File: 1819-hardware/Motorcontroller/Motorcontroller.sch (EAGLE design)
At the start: 34 parts, among them U1 GENERIC-SOIC8MSGEQ7N-FILTER, U2 GENERIC-SOIC8MSGEQ7N-FILTER, U3 GENERIC-SOIC8MSGEQ7N-FILTER

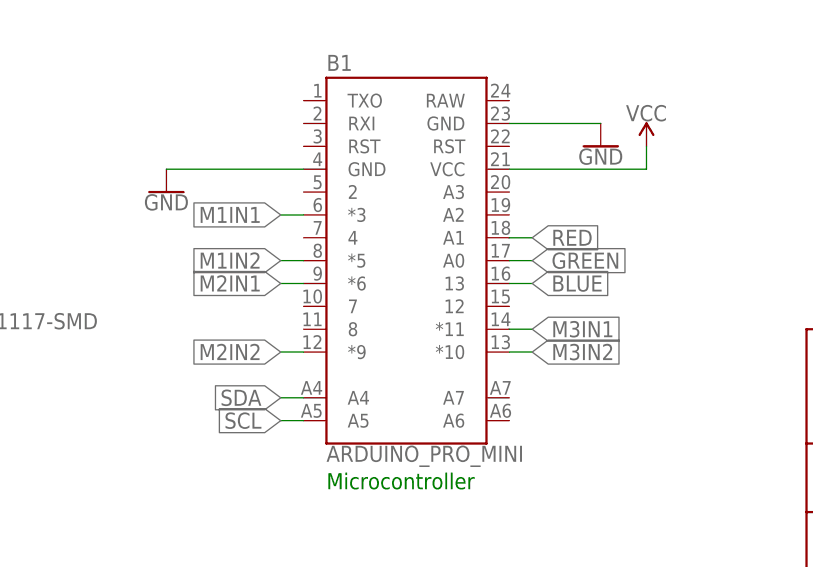
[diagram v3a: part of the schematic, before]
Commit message: the arduino was upside down
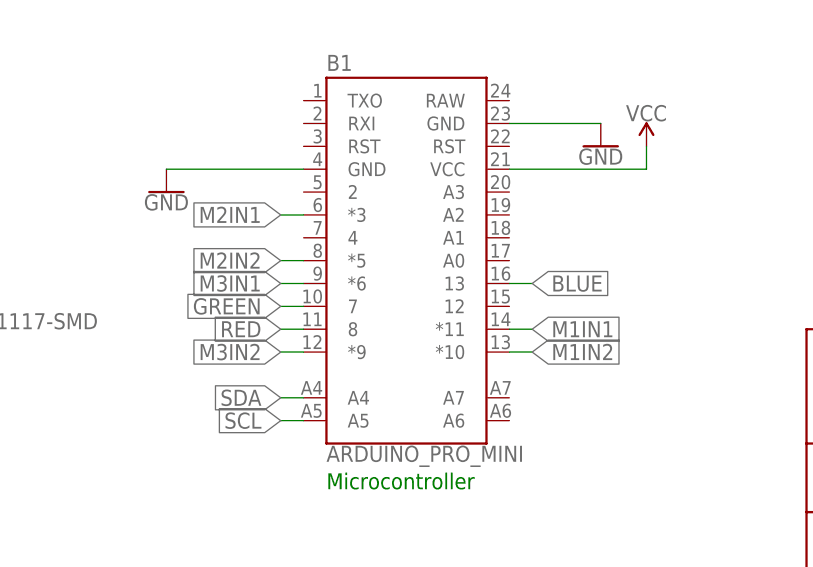
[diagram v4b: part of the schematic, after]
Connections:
- net GREEN: now also B1.7; no longer B1.A0
- net M1IN1: now also B1.*11; no longer B1.*3
- net M1IN2: now also B1.*10; no longer B1.*5
- net M2IN1: now also B1.*3; no longer B1.*6
- net M2IN2: now also B1.*5; no longer B1.*9
- net M3IN1: now also B1.*6; no longer B1.*11
- net M3IN2: now also B1.*9; no longer B1.*10
- net RED: now also B1.8; no longer B1.A1
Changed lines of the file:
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@@
 </segment>
 <segment>
-<pinref part="B1" gate="G$1" pin="A1"/>
-<wire x1="114.3" y1="45.72" x2="116.84" y2="45.72" width="0.1524" layer="91"/>
-<label x="116.84" y="45.72" size="1.778" layer="95" xref="yes"/>
+<pinref part="B1" gate="G$1" pin="8"/>
+<wire x1="91.44" y1="35.56" x2="88.9" y2="35.56" width="0.1524" layer="91"/>
+<label x="88.9" y="35.56" size="1.778" layer="95" rot="R180" xref="yes"/>
 </segment>
 </net>
@@
 </segment>
 <segment>
-<pinref part="B1" gate="G$1" pin="A0"/>
-<wire x1="114.3" y1="43.18" x2="116.84" y2="43.18" width="0.1524" layer="91"/>
-<label x="116.84" y="43.18" size="1.778" layer="95" xref="yes"/>
+<pinref part="B1" gate="G$1" pin="7"/>
+<wire x1="91.44" y1="38.1" x2="88.9" y2="38.1" width="0.1524" layer="91"/>
+<label x="88.9" y="38.1" size="1.778" layer="95" rot="R180" xref="yes"/>
 </segment>
 </net>
@@
 <net name="M1IN1" class="0">
 <segment>
-<pinref part="B1" gate="G$1" pin="*3"/>
-<wire x1="91.44" y1="48.26" x2="88.9" y2="48.26" width="0.1524" layer="91"/>
-<label x="88.9" y="48.26" size="1.778" layer="95" rot="R180" xref="yes"/>
-</segment>
-<segment>
 <pinref part="U1" gate="G$1" pin="3"/>
 <wire x1="177.8" y1="162.56" x2="175.26" y2="162.56" width="0.1524" layer="91"/>
 <label x="175.26" y="162.56" size="1.778" layer="95" rot="R180" xref="yes"/>
 </segment>
+<segment>
+<pinref part="B1" gate="G$1" pin="*11"/>
+<wire x1="114.3" y1="35.56" x2="116.84" y2="35.56" width="0.1524" layer="91"/>
+<label x="116.84" y="35.56" size="1.778" layer="95" xref="yes"/>
+</segment>
 </net>
 <net name="M1IN2" class="0">
-<segment>
-<pinref part="B1" gate="G$1" pin="*5"/>
-<wire x1="91.44" y1="43.18" x2="88.9" y2="43.18" width="0.1524" layer="91"/>
-<label x="88.9" y="43.18" size="1.778" layer="95" rot="R180" xref="yes"/>
-</segment>
 <segment>
 <pinref part="U1" gate="G$1" pin="2"/>
@@
 <label x="175.26" y="165.1" size="1.778" layer="95" rot="R180" xref="yes"/>
 </segment>
+<segment>
+<pinref part="B1" gate="G$1" pin="*10"/>
+<wire x1="114.3" y1="33.02" x2="116.84" y2="33.02" width="0.1524" layer="91"/>
+<label x="116.84" y="33.02" size="1.778" layer="95" xref="yes"/>
+</segment>
 </net>
 <net name="M2IN1" class="0">
-<segment>
-<pinref part="B1" gate="G$1" pin="*6"/>
-<wire x1="91.44" y1="40.64" x2="88.9" y2="40.64" width="0.1524" layer="91"/>
-<label x="88.9" y="40.64" size="1.778" layer="95" rot="R180" xref="yes"/>
-</segment>
 <segment>
 <pinref part="U2" gate="G$1" pin="3"/>
@@
 <label x="175.26" y="119.38" size="1.778" layer="95" rot="R180" xref="yes"/>
 </segment>
+<segment>
+<pinref part="B1" gate="G$1" pin="*3"/>
+<wire x1="91.44" y1="48.26" x2="88.9" y2="48.26" width="0.1524" layer="91"/>
+<label x="88.9" y="48.26" size="1.778" layer="95" rot="R180" xref="yes"/>
+</segment>
 </net>
 <net name="M2IN2" class="0">
-<segment>
-<pinref part="B1" gate="G$1" pin="*9"/>
-<wire x1="91.44" y1="33.02" x2="88.9" y2="33.02" width="0.1524" layer="91"/>
-<label x="88.9" y="33.02" size="1.778" layer="95" rot="R180" xref="yes"/>
-</segment>
 <segment>
 <pinref part="U2" gate="G$1" pin="2"/>
 <wire x1="177.8" y1="121.92" x2="175.26" y2="121.92" width="0.1524" layer="91"/>
 <label x="175.26" y="121.92" size="1.778" layer="95" rot="R180" xref="yes"/>
+</segment>
+<segment>
+<pinref part="B1" gate="G$1" pin="*5"/>
+<wire x1="91.44" y1="43.18" x2="88.9" y2="43.18" width="0.1524" layer="91"/>
+<label x="88.9" y="43.18" size="1.778" layer="95" rot="R180" xref="yes"/>
 </segment>
 </net>
@@
 </segment>
 <segment>
-<pinref part="B1" gate="G$1" pin="*11"/>
-<wire x1="114.3" y1="35.56" x2="116.84" y2="35.56" width="0.1524" layer="91"/>
-<label x="116.84" y="35.56" size="1.778" layer="95" xref="yes"/>
+<pinref part="B1" gate="G$1" pin="*6"/>
+<wire x1="91.44" y1="40.64" x2="88.9" y2="40.64" width="0.1524" layer="91"/>
+<label x="88.9" y="40.64" size="1.778" layer="95" rot="R180" xref="yes"/>
 </segment>
 </net>
@@
 </segment>
 <segment>
-<pinref part="B1" gate="G$1" pin="*10"/>
-<wire x1="114.3" y1="33.02" x2="116.84" y2="33.02" width="0.1524" layer="91"/>
-<label x="116.84" y="33.02" size="1.778" layer="95" xref="yes"/>
+<pinref part="B1" gate="G$1" pin="*9"/>
+<wire x1="91.44" y1="33.02" x2="88.9" y2="33.02" width="0.1524" layer="91"/>
+<label x="88.9" y="33.02" size="1.778" layer="95" rot="R180" xref="yes"/>
 </segment>
 </net>

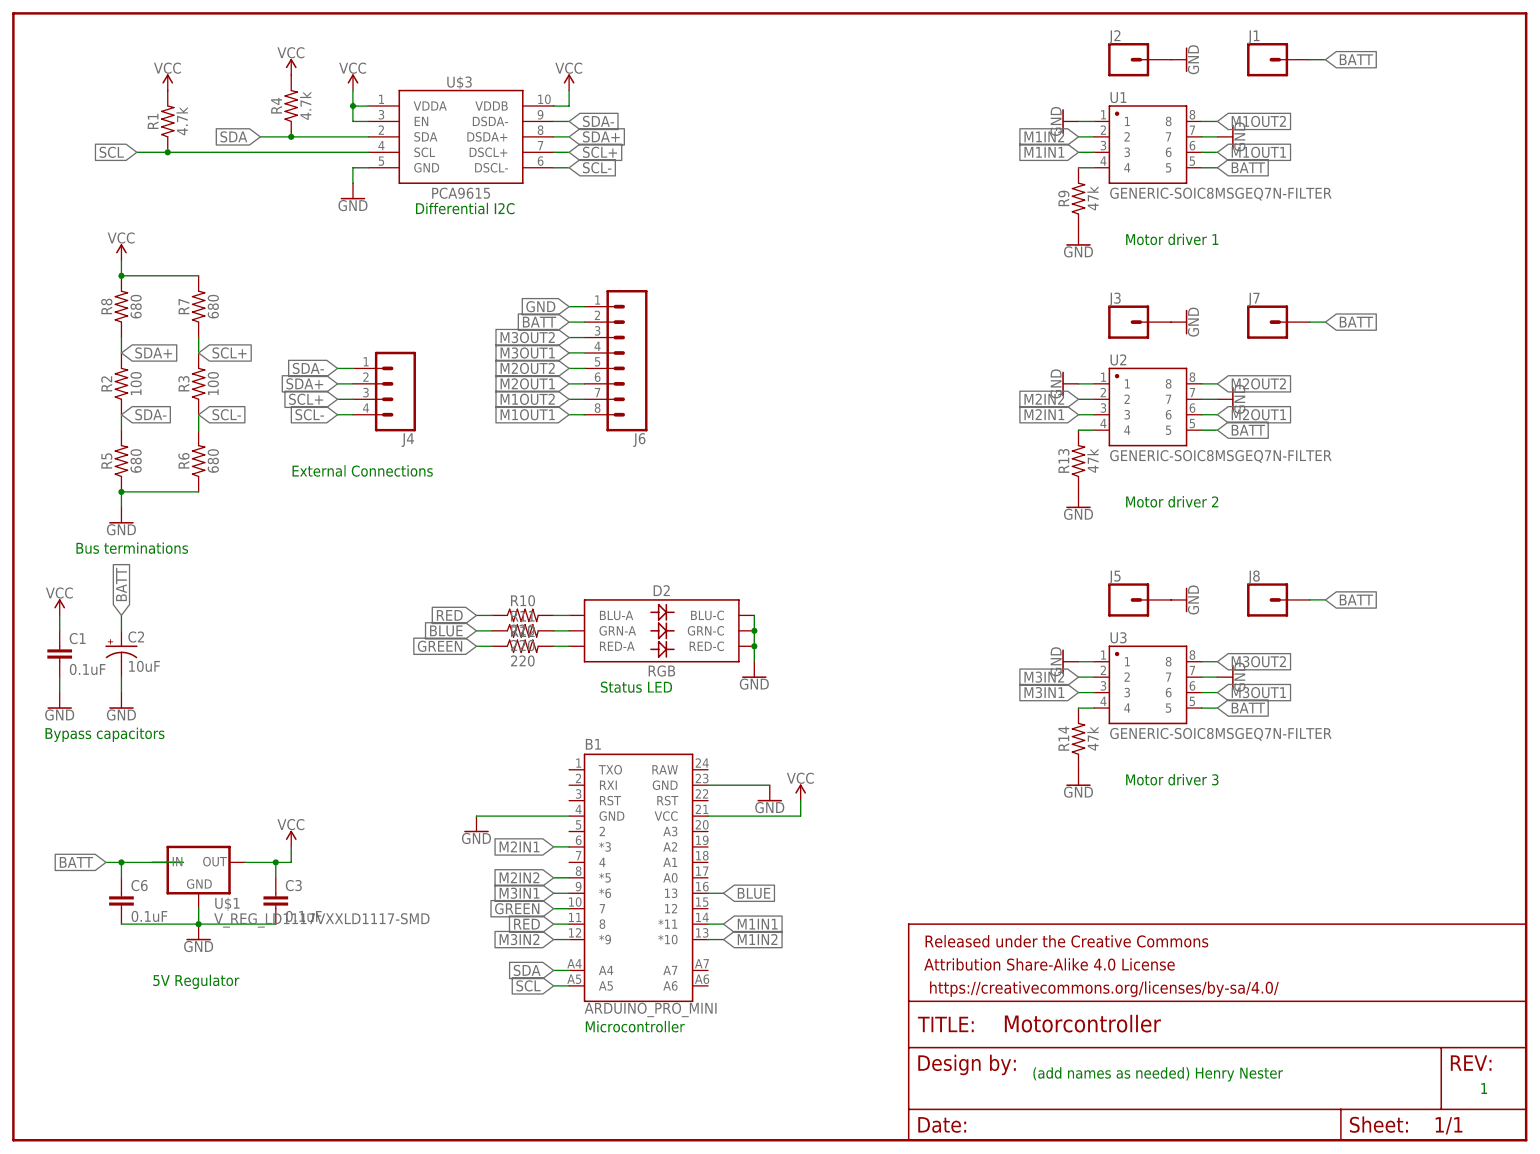
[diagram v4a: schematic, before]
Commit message: work on motorcontroller pcbs
switching arduino to an i2c device that provides 16 pwm outputs. this will reduce costs and simplify code since we only need one firmware written
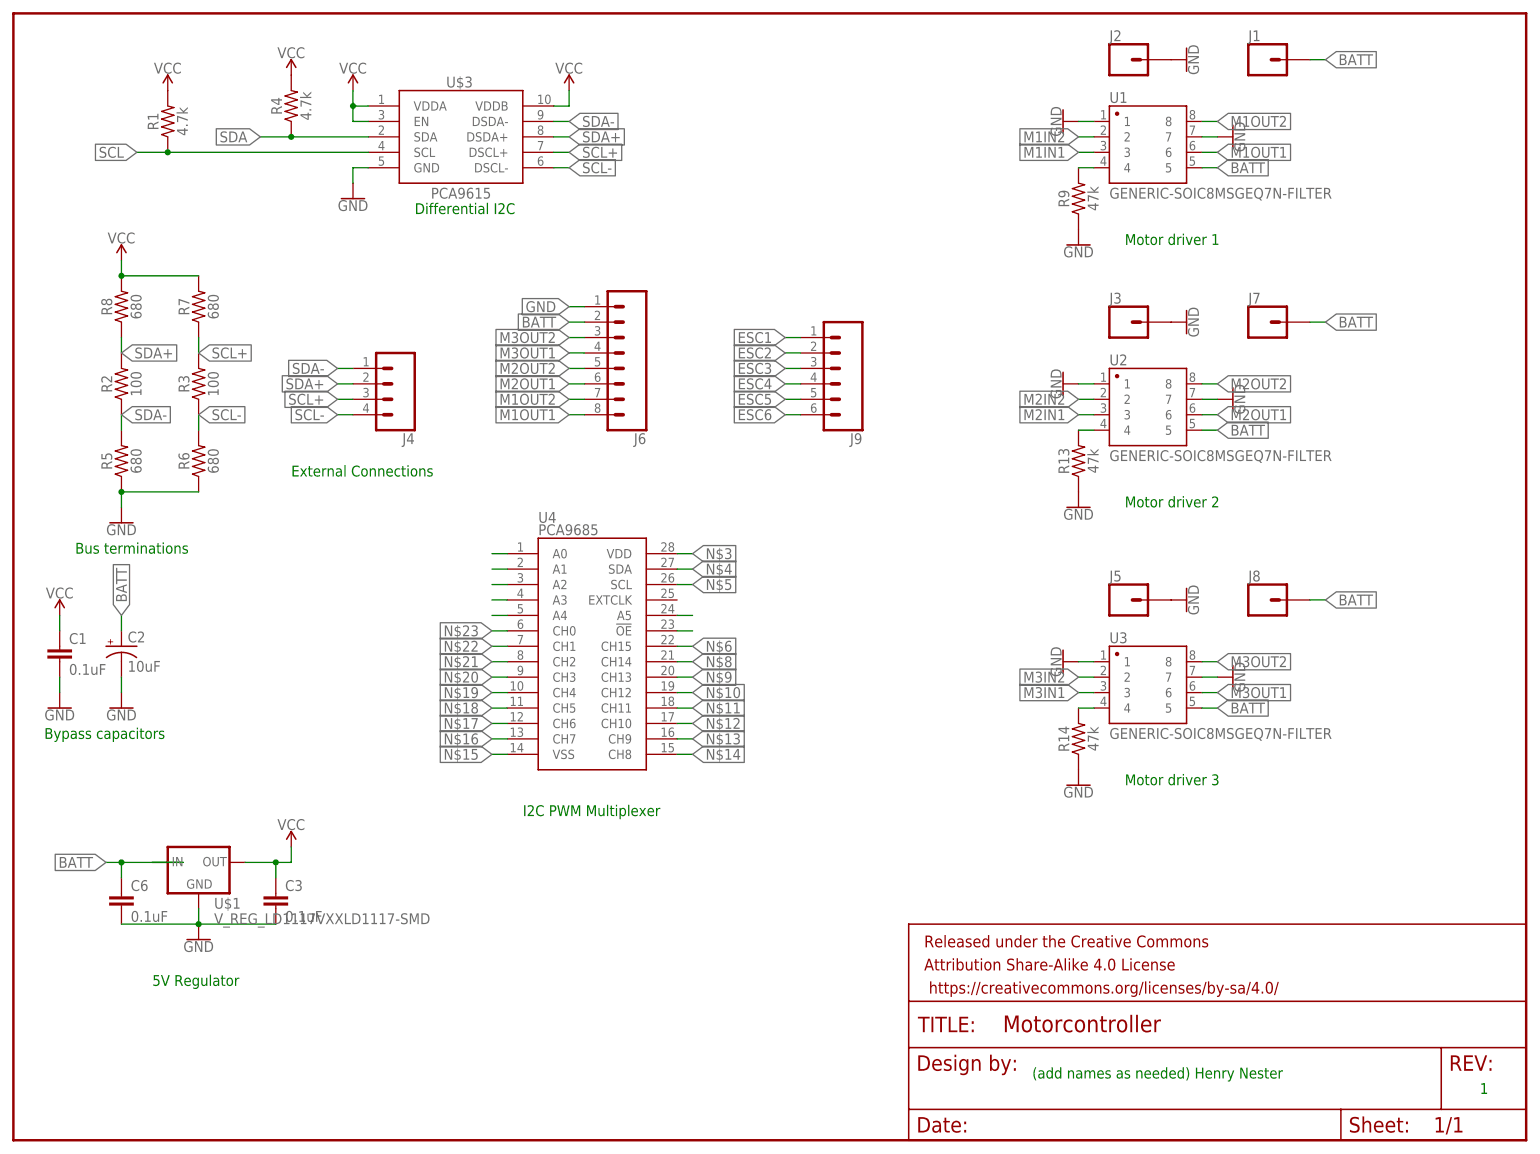
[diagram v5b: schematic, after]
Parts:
- removed B1: ARDUINO_PRO_MINI, SparkFun-Boards:ARDUINO_PRO_MINI
- removed D2: RGB, SparkFun-LED:LED-RGBPLCC-6
- removed R10, R11, R12: 220, SparkFun-Resistors:220OHM-0603-1/10W-1%
- added J9: (no value), SparkFun-Connectors:CONN_06SILK_FEMALE_PTH
- added U4: PCA9685, SparkFun-IC-Special-Function:PCA9685
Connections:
- removed net BLUE: B1.13, R11.1
- removed net GREEN: B1.7, R12.1
- removed net RED: B1.8, R10.1
- new net ESC1: J9.1
- new net ESC2: J9.2
- new net ESC3: J9.3
- new net ESC4: J9.4
- new net ESC5: J9.5
- new net ESC6: J9.6
- new net N$10: U4.CH12
- new net N$11: U4.CH11
- new net N$12: U4.CH10
- new net N$13: U4.CH9
- new net N$14: U4.CH8
- new net N$15: U4.VSS
- new net N$16: U4.CH7
- new net N$17: U4.CH6
- new net N$18: U4.CH5
- new net N$19: U4.CH4
- new net N$20: U4.CH3
- new net N$21: U4.CH2
- new net N$22: U4.CH1
- new net N$23: U4.CH0
- new net N$24: U4.A4
- new net N$25: U4.A3
- new net N$26: U4.A2
- new net N$27: U4.A1
- new net N$28: U4.A0
- new net N$29: U4.A5
- new net N$3: U4.VDD
- new net N$30: U4.!OE
- new net N$8: U4.CH14
- new net N$9: U4.CH13
- net GND: no longer B1.GND, B1.GND@2, D2.BLU-C, D2.GRN-C, D2.RED-C
- net M1IN1: no longer B1.*11
- net M1IN2: no longer B1.*10
- net M2IN1: no longer B1.*3
- net M2IN2: no longer B1.*5
- net M3IN1: no longer B1.*6
- net M3IN2: no longer B1.*9
- net N$4: now also U4.SDA; no longer D2.BLU-A, R10.2
- net N$5: now also U4.SCL; no longer D2.GRN-A, R11.2
- net N$6: now also U4.CH15; no longer D2.RED-A, R12.2
- net SCL: no longer B1.A5
- net SDA: no longer B1.A4
- net VCC: no longer B1.VCC
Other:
- note added: "I2C PWM Multiplexer"
- note removed: "Microcontroller"
- note removed: "Status LED"
